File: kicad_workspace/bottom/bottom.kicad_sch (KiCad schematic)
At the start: 50 parts, among them J1 Battery connector, J2 Battery connector, M1 N20_MOTOR_EXTENDED_SHAFT, M2 N20_MOTOR_EXTENDED_SHAFT, U1 DRV8833PWP, U3 STM32F303RETx, U4 BNO055, Y1 32.768kHz, Y2 8MHz, Y3 32.768kHz

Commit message: add mounting holes and acs712 current sensors to schematic
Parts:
- added C22, C23: 100nF, Capacitor_SMD:C_0805_2012Metric, symbol Device:C
- added H1, H2, H3, H4: MountingHole, symbol Mechanical:MountingHole
- added R10, R11, R12, R13: 10K, Resistor_SMD:R_0805_2012Metric, symbol Device:R
- added U12, U13: ACS712-5A, Package_SO:SOIC-8_3.9x4.9mm_P1.27mm, symbol Sensor_Current:ACS712xLCTR-05B
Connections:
- net +5V: now also U12.8 (VCC), U13.8 (VCC)
- net GND: now also C22.2, C23.2, R11.1, R13.1, U12.5 (GND), U13.5 (GND)
- net IP_MOTOR_A+: now reaches M1.5 (M2)
- net IP_MOTOR_A+: now also U13.1 (IP+), U13.2 (IP+); no longer U1.4 (AOUT2)
- net IP_MOTOR_B+: now reaches M2.5 (M2)
- net IP_MOTOR_B+: now also U12.1 (IP+), U12.2 (IP+); no longer U1.5 (BOUT2)
- new net: C22.1, U12.6 (FILTER)
- new net: R12.2, U12.7 (VIOUT)
- new net: R10.2, U13.7 (VIOUT)
- new net: C23.1, U13.6 (FILTER)
- new net IP_MOTOR_A-: U1.4 (AOUT2), U13.3 (IP-), U13.4 (IP-)
- new net IP_MOTOR_B-: U1.5 (BOUT2), U12.3 (IP-), U12.4 (IP-)
- new net I_MOTOR_A: R10.1, R11.2
- new net I_MOTOR_B: R12.1, R13.2
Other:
- moved on the sheet: C1, C10, C11, C12, C13, C14, C15, C16, C17, C18, C19, C2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

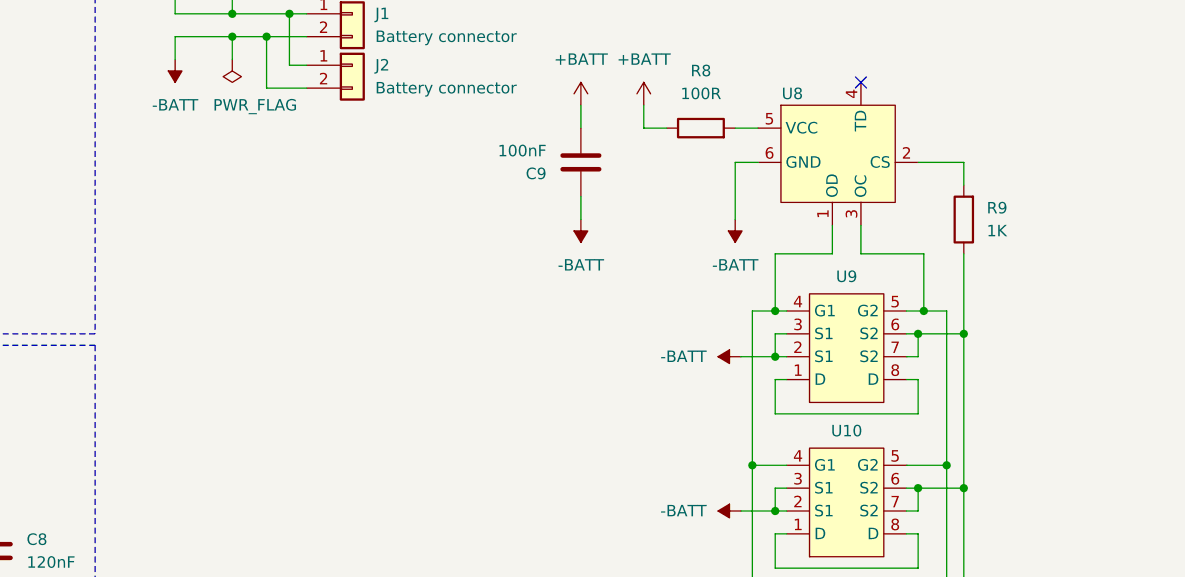
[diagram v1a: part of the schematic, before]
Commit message: add S7V8F3 symbol, footprint. add S7V8F3 to schematic
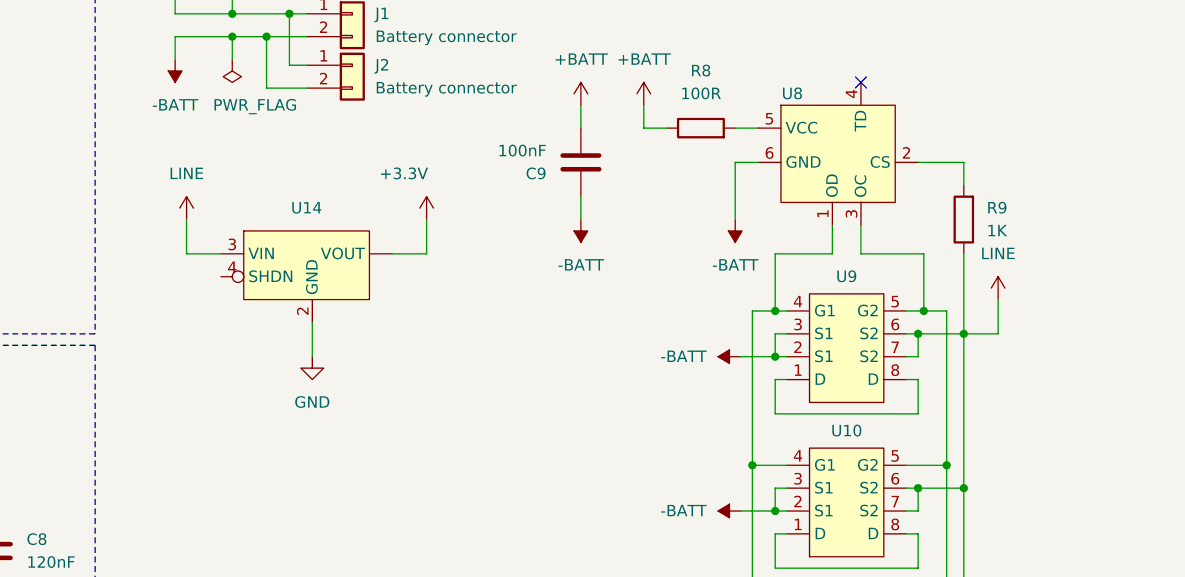
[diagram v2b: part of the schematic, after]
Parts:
- added U14: ~, pololu:S7V8F3, symbol pololu:S7V8F3
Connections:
- net +3.3V: now also U14. (VOUT)
- net GND: now also U14.2 (GND)
- net LINE: now reaches R9.1, U10.6 (S2), U10.7 (S2), U11.6 (S2), U11.7 (S2), U2.6 (S2), U2.7 (S2), U9.6 (S2), U9.7 (S2)
- net LINE: now also U14.3 (VIN)
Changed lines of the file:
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@@
     (stroke (width 0) (type default))
   )
+  (wire (pts (xy 264.16 48.26) (xy 264.16 52.07))
+    (stroke (width 0) (type default))
+  )
   (wire (pts (xy 330.835 100.33) (xy 329.565 100.33))
     (stroke (width 0) (type default))
@@
     (stroke (width 0) (type default))
   )
+  (wire (pts (xy 264.16 52.07) (xy 267.97 52.07))
+    (stroke (width 0) (type default))
+  )
   (wire (pts (xy 212.09 182.88) (xy 215.9 182.88))
     (stroke (width 0) (type default))
@@
     (stroke (width 0) (type default))
   )
+  (wire (pts (xy 354.33 60.96) (xy 350.52 60.96))
+    (stroke (width 0) (type default))
+  )
   (wire (pts (xy 40.005 57.15) (xy 38.735 57.15))
     (stroke (width 0) (type default))
@@
     (stroke (width 0) (type default))
   )
+  (wire (pts (xy 290.83 52.07) (xy 290.83 48.26))
+    (stroke (width 0) (type default))
+  )
   (wire (pts (xy 210.82 90.17) (xy 210.82 92.71))
     (stroke (width 0) (type default))
@@
     (stroke (width 0) (type default))
   )
+  (wire (pts (xy 354.33 57.15) (xy 354.33 60.96))
+    (stroke (width 0) (type default))
+  )
   (wire (pts (xy 330.835 95.25) (xy 329.565 95.25))
     (stroke (width 0) (type default))
@@
     (stroke (width 0) (type default))
   )
+  (wire (pts (xy 278.13 59.69) (xy 278.13 63.5))
+    (stroke (width 0) (type default))
+  )
   (wire (pts (xy 92.075 102.235) (xy 95.885 102.235))
     (stroke (width 0) (type default))
@@
     (stroke (width 0) (type default))
   )
+  (wire (pts (xy 287.02 52.07) (xy 290.83 52.07))
+    (stroke (width 0) (type default))
+  )
   (wire (pts (xy 329.565 83.185) (xy 329.565 86.995))
     (stroke (width 0) (type default))
@@
     )
   )
+  (symbol (lib_id "power:LINE") (at 354.33 57.15 0) (unit 1)
+    (in_bom yes) (on_board yes) (dnp no) (fields_autoplaced)
+    (property "Reference" "#PWR070" (at 354.33 60.96 0)
+      (effects (font (size 1.27 1.27)) hide)
+    )
+    (property "Value" "LINE" (at 354.33 52.07 0)
+      (effects (font (size 1.27 1.27)))
+    )
+    (property "Footprint" "" (at 354.33 57.15 0)
+      (effects (font (size 1.27 1.27)) hide)
+    )
+    (property "Datasheet" "" (at 354.33 57.15 0)
+      (effects (font (size 1.27 1.27)) hide)
+    )
+    (pin "1")
+    (instances
+      (project "bottom"
+        (path "/8949e4cc-98fb-401d-bf78-7a26c685fd98"
+          (reference "#PWR070") (unit 1)
+        )
+      )
+    )
+  )
   (symbol (lib_id "pololu:8205A") (at 333.375 85.725 0) (mirror x) (unit 1)
     (in_bom yes) (on_board yes) (dnp no)
@@
     )
   )
+  (symbol (lib_id "power:GND") (at 278.13 63.5 0) (mirror y) (unit 1)
+    (in_bom yes) (on_board yes) (dnp no) (fields_autoplaced)
+    (property "Reference" "#PWR069" (at 278.13 69.85 0)
+      (effects (font (size 1.27 1.27)) hide)
+    )
+    (property "Value" "GND" (at 278.13 68.58 0)
+      (effects (font (size 1.27 1.27)))
+    )
+    (property "Footprint" "" (at 278.13 63.5 0)
+      (effects (font (size 1.27 1.27)) hide)
+    )
+    (property "Datasheet" "" (at 278.13 63.5 0)
+      (effects (font (size 1.27 1.27)) hide)
+    )
+    (pin "1")
+    (instances
+      (project "bottom"
+        (path "/8949e4cc-98fb-401d-bf78-7a26c685fd98"
+          (reference "#PWR069") (unit 1)
+        )
+      )
+    )
+  )
   (symbol (lib_id "power:GND") (at 118.11 34.29 0) (unit 1)
     (in_bom yes) (on_board yes) (dnp no) (fields_autoplaced)
@@
     )
   )
+  (symbol (lib_id "power:+3.3V") (at 290.83 48.26 0) (unit 1)
+    (in_bom yes) (on_board yes) (dnp no)
+    (property "Reference" "#PWR072" (at 290.83 52.07 0)
+      (effects (font (size 1.27 1.27)) hide)
+    )
+    (property "Value" "+3.3V" (at 288.29 43.18 0)
+      (effects (font (size 1.27 1.27)))
+    )
+    (property "Footprint" "" (at 290.83 48.26 0)
+      (effects (font (size 1.27 1.27)) hide)
+    )
+    (property "Datasheet" "" (at 290.83 48.26 0)
+      (effects (font (size 1.27 1.27)) hide)
+    )
+    (pin "1")
+    (instances
+      (project "bottom"
+        (path "/8949e4cc-98fb-401d-bf78-7a26c685fd98"
+          (reference "#PWR072") (unit 1)
+        )
+      )
+    )
+  )
   (symbol (lib_id "power:GND") (at 210.82 128.27 0) (mirror y) (unit 1)
     (in_bom yes) (on_board yes) (dnp no) (fields_autoplaced)
@@
     )
   )
+  (symbol (lib_id "pololu:S7V8F3") (at 270.51 49.53 0) (unit 1)
+    (in_bom yes) (on_board yes) (dnp no) (fields_autoplaced)
+    (property "Reference" "U14" (at 277.495 46.99 0)
+      (effects (font (size 1.27 1.27)))
+    )
+    (property "Value" "~" (at 270.51 49.53 0)
+      (effects (font (size 1.27 1.27)))
+    )
+    (property "Footprint" "pololu:S7V8F3" (at 280.67 48.26 0)
+      (effects (font (size 1.27 1.27)) hide)
+    )
+    (property "Datasheet" "" (at 270.51 49.53 0)
+      (effects (font (size 1.27 1.27)) hide)
+    )
+    (pin "2")
+    (pin "3")
+    (pin "4")
+    (pin "")
+    (instances
+      (project "bottom"
+        (path "/8949e4cc-98fb-401d-bf78-7a26c685fd98"
+          (reference "U14") (unit 1)
+        )
+      )
+    )
+  )
   (symbol (lib_id "Device:Crystal") (at 50.165 100.965 270) (mirror x) (unit 1)
     (in_bom yes) (on_board yes) (dnp no)
@@
         )
       )
+    )
+  )
+  (symbol (lib_id "power:LINE") (at 264.16 48.26 0) (unit 1)
+    (in_bom yes) (on_board yes) (dnp no) (fields_autoplaced)
+    (property "Reference" "#PWR071" (at 264.16 52.07 0)
+      (effects (font (size 1.27 1.27)) hide)
+    )
+    (property "Value" "LINE" (at 264.16 43.18 0)
+      (effects (font (size 1.27 1.27)))
+    )
+    (property "Footprint" "" (at 264.16 48.26 0)
+      (effects (font (size 1.27 1.27)) hide)
+    )
+    (property "Datasheet" "" (at 264.16 48.26 0)
+      (effects (font (size 1.27 1.27)) hide)
+    )
+    (pin "1")
+    (instances
+      (project "bottom"
+        (path "/8949e4cc-98fb-401d-bf78-7a26c685fd98"
+          (reference "#PWR071") (unit 1)
+        )
+      )

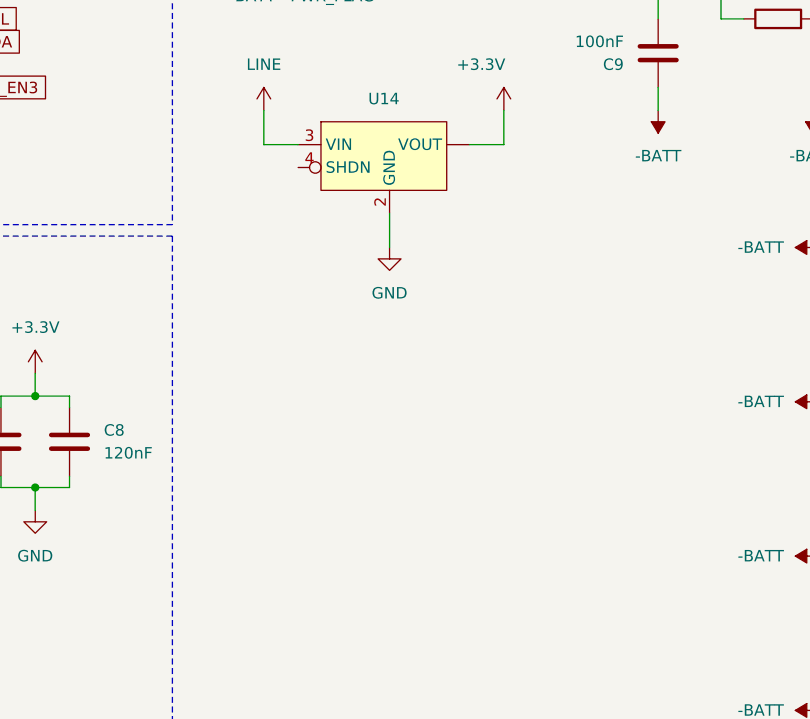
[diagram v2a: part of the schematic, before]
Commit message: add U3V70F5 symbol and footprint. add it to schematic
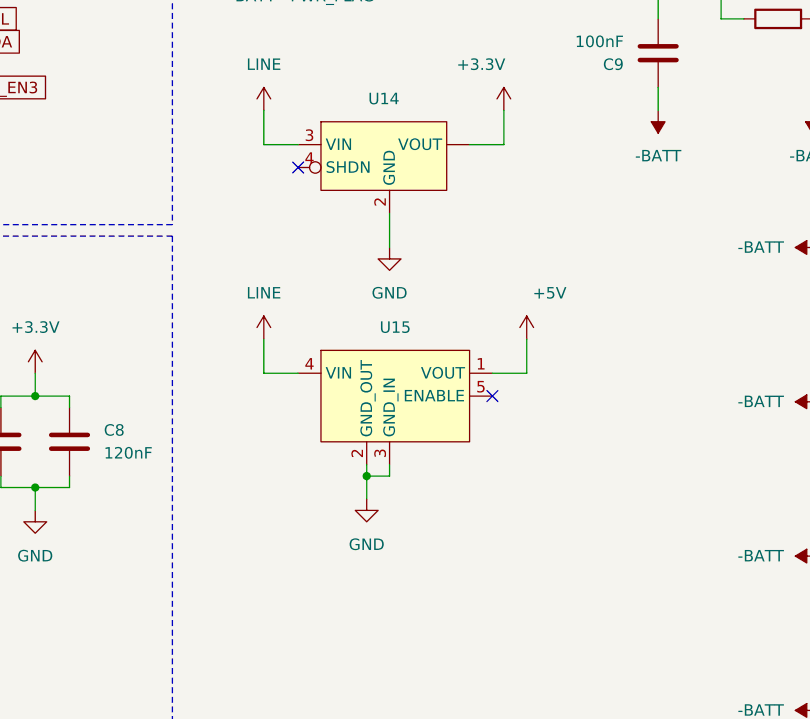
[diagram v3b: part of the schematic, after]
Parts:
- added U15: ~, pololu:U3V70F5, symbol pololu:U3V70F5
- U14: footprint pololu:S7V8F3 -> pololu:S7V8F3_vertical
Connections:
- net +5V: now also U15.1 (VOUT)
- net GND: now also U15.2 (GND_OUT), U15.3 (GND_IN)
- net LINE: now also U15.4 (VIN)
- no-connect marks 41 -> 43
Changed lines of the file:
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@@
   (junction (at 329.565 63.5) (diameter 0) (color 0 0 0 0)
   )
+  (junction (at 275.59 88.9) (diameter 0) (color 0 0 0 0)
+  )
   (junction (at 275.59 25.4) (diameter 0) (color 0 0 0 0)
   )
@@
   (no_connect (at 224.79 43.18))
   (no_connect (at 92.075 69.215))
+  (no_connect (at 289.56 80.01))
   (no_connect (at 92.075 120.015))
   (no_connect (at 56.515 86.995))
+  (no_connect (at 267.97 54.61))
   (no_connect (at 92.075 94.615))
   (no_connect (at 56.515 84.455))
@@
     (stroke (width 0) (type default))
   )
+  (wire (pts (xy 278.13 87.63) (xy 278.13 88.9))
+    (stroke (width 0) (type default))
+  )
   (wire (pts (xy 97.79 61.595) (xy 103.505 61.595))
     (stroke (width 0) (type default))
@@
     (stroke (width 0) (type default))
   )
+  (wire (pts (xy 278.13 88.9) (xy 275.59 88.9))
+    (stroke (width 0) (type default))
+  )
   (wire (pts (xy 327.025 92.71) (xy 327.025 109.855))
     (stroke (width 0) (type default))
@@
     (stroke (width 0) (type default))
   )
+  (wire (pts (xy 293.37 77.47) (xy 293.37 73.66))
+    (stroke (width 0) (type default))
+  )
   (wire (pts (xy 74.295 131.445) (xy 74.295 132.715))
     (stroke (width 0) (type default))
@@
     (stroke (width 0) (type default))
   )
+  (wire (pts (xy 264.16 73.66) (xy 264.16 77.47))
+    (stroke (width 0) (type default))
+  )
   (wire (pts (xy 177.8 180.34) (xy 181.61 180.34))
     (stroke (width 0) (type default))
@@
     (stroke (width 0) (type default))
   )
+  (wire (pts (xy 275.59 87.63) (xy 275.59 88.9))
+    (stroke (width 0) (type default))
+  )
   (wire (pts (xy 153.67 121.92) (xy 156.21 121.92))
     (stroke (width 0) (type default))
@@
     (stroke (width 0) (type default))
   )
+  (wire (pts (xy 275.59 88.9) (xy 275.59 91.44))
+    (stroke (width 0) (type default))
+  )
   (wire (pts (xy 346.075 58.42) (xy 344.17 58.42))
     (stroke (width 0) (type default))
@@
     (stroke (width 0) (type default))
   )
+  (wire (pts (xy 289.56 77.47) (xy 293.37 77.47))
+    (stroke (width 0) (type default))
+  )
   (wire (pts (xy 172.72 35.56) (xy 172.72 50.8))
     (stroke (width 0) (type default))
@@
     (stroke (width 0) (type default))
   )
+  (wire (pts (xy 264.16 77.47) (xy 267.97 77.47))
+    (stroke (width 0) (type default))
+  )
   (wire (pts (xy 208.28 90.17) (xy 210.82 90.17))
     (stroke (width 0) (type default))
@@
     )
   )
+  (symbol (lib_id "power:+5V") (at 293.37 73.66 0) (unit 1)
+    (in_bom yes) (on_board yes) (dnp no)
+    (property "Reference" "#PWR074" (at 293.37 77.47 0)
+      (effects (font (size 1.27 1.27)) hide)
+    )
+    (property "Value" "+5V" (at 295.91 68.58 0)
+      (effects (font (size 1.27 1.27)))
+    )
+    (property "Footprint" "" (at 293.37 73.66 0)
+      (effects (font (size 1.27 1.27)) hide)
+    )
+    (property "Datasheet" "" (at 293.37 73.66 0)
+      (effects (font (size 1.27 1.27)) hide)
+    )
+    (pin "1")
+    (instances
+      (project "bottom"
+        (path "/8949e4cc-98fb-401d-bf78-7a26c685fd98"
+          (reference "#PWR074") (unit 1)
+        )
+      )
+    )
+  )
+  (symbol (lib_id "power:LINE") (at 264.16 73.66 0) (unit 1)
+    (in_bom yes) (on_board yes) (dnp no) (fields_autoplaced)
+    (property "Reference" "#PWR073" (at 264.16 77.47 0)
+      (effects (font (size 1.27 1.27)) hide)
+    )
+    (property "Value" "LINE" (at 264.16 68.58 0)
+      (effects (font (size 1.27 1.27)))
+    )
+    (property "Footprint" "" (at 264.16 73.66 0)
+      (effects (font (size 1.27 1.27)) hide)
+    )
+    (property "Datasheet" "" (at 264.16 73.66 0)
+      (effects (font (size 1.27 1.27)) hide)
+    )
+    (pin "1")
+    (instances
+      (project "bottom"
+        (path "/8949e4cc-98fb-401d-bf78-7a26c685fd98"
+          (reference "#PWR073") (unit 1)
+        )
+      )
+    )
+  )
   (symbol (lib_id "Device:R") (at 175.26 83.82 180) (unit 1)
     (in_bom yes) (on_board yes) (dnp no) (fields_autoplaced)
@@
     )
   )
+  (symbol (lib_id "pololu:U3V70F5") (at 270.51 74.93 0) (unit 1)
+    (in_bom yes) (on_board yes) (dnp no) (fields_autoplaced)
+    (property "Reference" "U15" (at 278.765 72.39 0)
+      (effects (font (size 1.27 1.27)))
+    )
+    (property "Value" "~" (at 270.51 74.93 0)
+      (effects (font (size 1.27 1.27)))
+    )
+    (property "Footprint" "pololu:U3V70F5" (at 280.67 73.66 0)
+      (effects (font (size 1.27 1.27)) hide)
+    )
+    (property "Datasheet" "" (at 270.51 74.93 0)
+      (effects (font (size 1.27 1.27)) hide)
+    )
+    (pin "2")
+    (pin "3")
+    (pin "4")
+    (pin "1")
+    (pin "5")
+    (instances
+      (project "bottom"
+        (path "/8949e4cc-98fb-401d-bf78-7a26c685fd98"
+          (reference "U15") (unit 1)
+        )
+      )
+    )
+  )
   (symbol (lib_id "Device:R") (at 350.52 48.26 180) (unit 1)
     (in_bom yes) (on_board yes) (dnp no) (fields_autoplaced)
@@
       (effects (font (size 1.27 1.27)))
     )
-    (property "Footprint" "pololu:S7V8F3" (at 280.67 48.26 0)
+    (property "Footprint" "pololu:S7V8F3_vertical" (at 280.67 48.26 0)
       (effects (font (size 1.27 1.27)) hide)
     )
@@
         )
       )
+    )
+  )
+  (symbol (lib_id "power:GND") (at 275.59 91.44 0) (mirror y) (unit 1)
+    (in_bom yes) (on_board yes) (dnp no) (fields_autoplaced)
+    (property "Reference" "#PWR075" (at 275.59 97.79 0)
+      (effects (font (size 1.27 1.27)) hide)
+    )
+    (property "Value" "GND" (at 275.59 96.52 0)
+      (effects (font (size 1.27 1.27)))
+    )
+    (property "Footprint" "" (at 275.59 91.44 0)
+      (effects (font (size 1.27 1.27)) hide)
+    )
+    (property "Datasheet" "" (at 275.59 91.44 0)
+      (effects (font (size 1.27 1.27)) hide)
+    )
+    (pin "1")
+    (instances
+      (project "bottom"
+        (path "/8949e4cc-98fb-401d-bf78-7a26c685fd98"
+          (reference "#PWR075") (unit 1)
+        )
+      )
